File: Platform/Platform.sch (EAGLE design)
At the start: 38 parts, among them U1 FT232RLSSOP, X1 USBSMD, Y1 RESONATORSMD

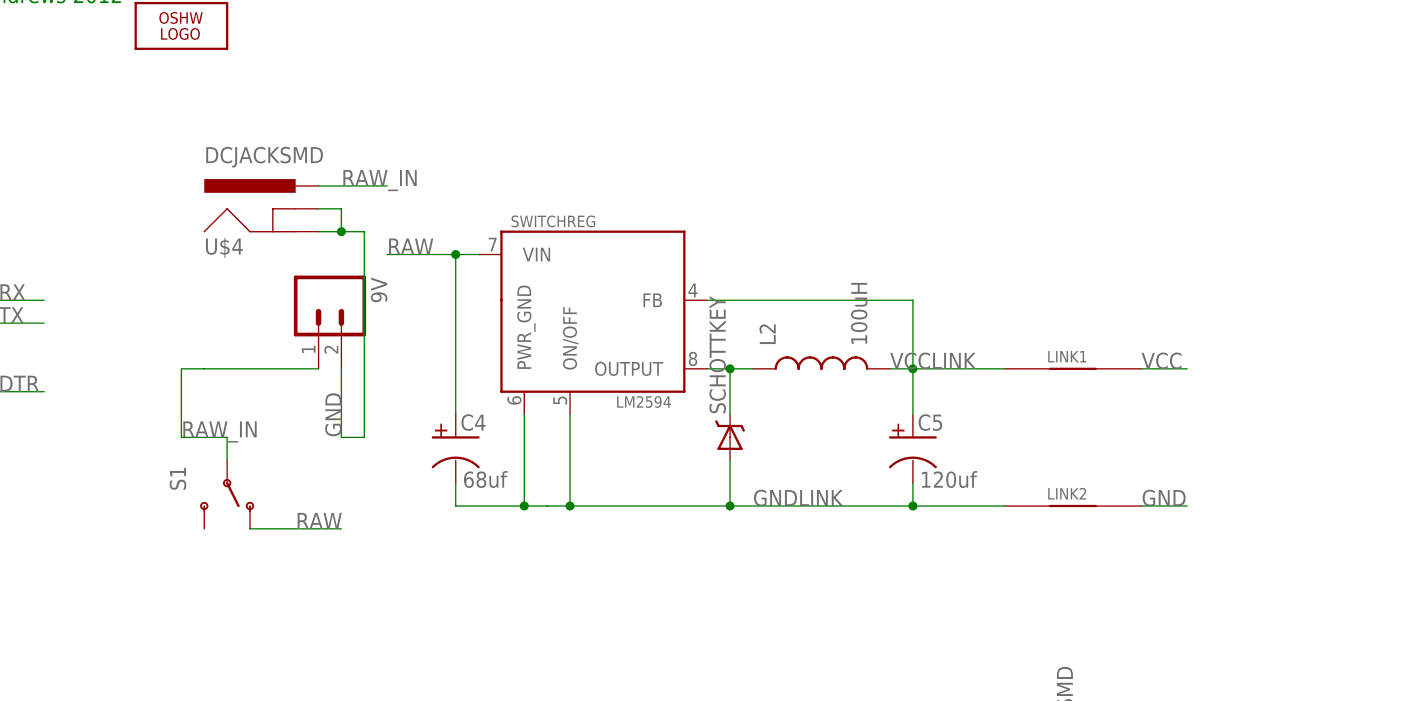
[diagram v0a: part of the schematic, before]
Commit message: switched back to LDO
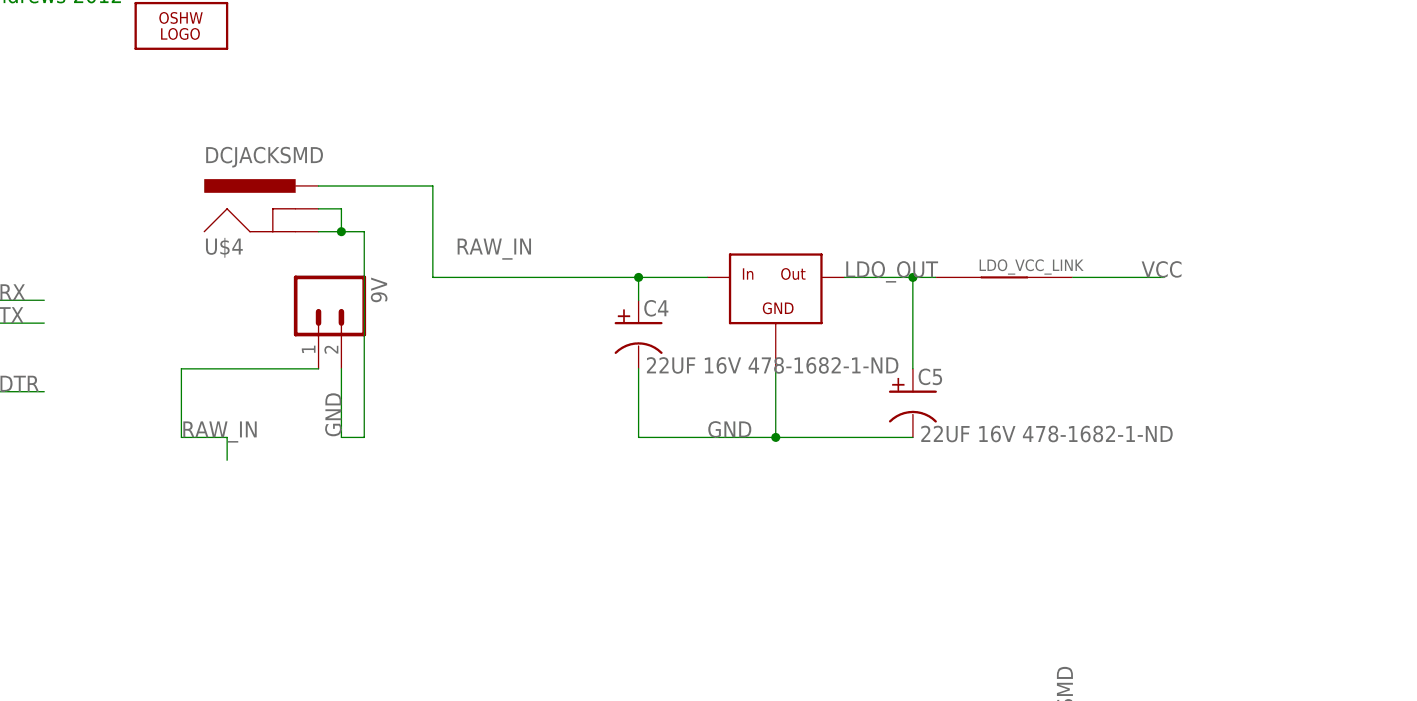
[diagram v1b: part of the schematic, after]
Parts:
- removed L2: 100uH, SparkFun:INDUCTOR0805
- removed LINK1, LINK2: LINK, Dustin:LINK
- removed S1: SWITCH-SPDT, Dustin:SWITCH-SPDT
- removed SCHOTTKEY: DIODE-SCHOTTKY, Dustin:DIODE-SCHOTTKY
- removed SWITCHREG: LM2594, Dustin:LM2594
- added LDO_VCC_LINK: LINK, Dustin:LINK
- added U$1: IFX25001TC, Dustin:IFX25001TC
- C4: value 68uf -> 22UF 16V 478-1682-1-ND; device Dustin:CAP_POLF80 -> Dustin:CAP_POL1210
- C5: value 120uf -> 22UF 16V 478-1682-1-ND; device Dustin:CAP_POL8X10 -> Dustin:CAP_POL1210
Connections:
- removed net GNDLINK: C4.-, C5.-, LINK2.P$1, SCHOTTKEY.A, SWITCHREG.ON/OFF, SWITCHREG.PWR_GND
- removed net N$3: L2.1, SCHOTTKEY.C, SWITCHREG.OUTPUT
- removed net RAW: C4.+, S1.O, SWITCHREG.VIN
- removed net VCCLINK: C5.+, L2.2, LINK1.P$1, SWITCHREG.FB
- new net LDO_OUT: C5.+, LDO_VCC_LINK.P$1, U$1.OUT
- net GND: now also C4.-, C5.-, U$1.GND; no longer LINK2.P$2
- net RAW_IN: now also C4.+, U$1.IN; no longer S1.P
- net VCC: now also LDO_VCC_LINK.P$2; no longer LINK1.P$2
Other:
- moved on the sheet: C4, C5

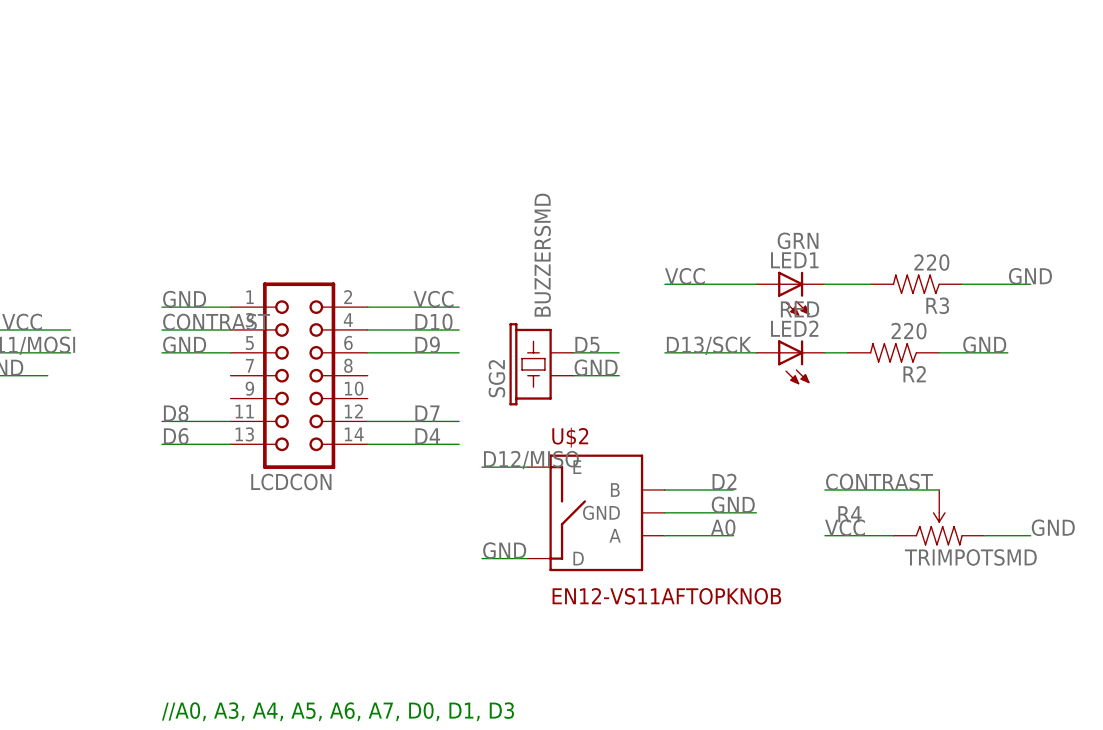
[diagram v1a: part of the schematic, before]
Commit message: wiring traces added
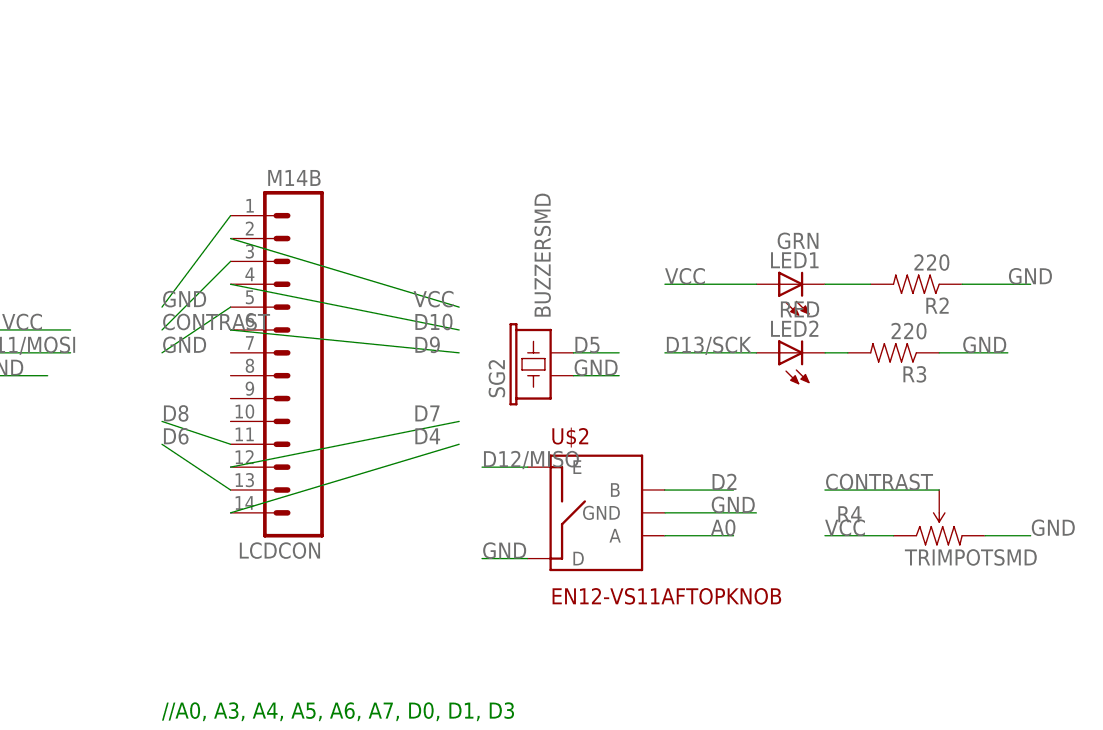
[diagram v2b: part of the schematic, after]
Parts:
- LCDCON: value (none) -> M14B; device con-harting:CON14 -> Dustin:M14B
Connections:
- net N$2: now also R3.2; no longer R2.2
- net N$7: now also R2.2; no longer R3.2
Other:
- moved on the sheet: LCDCON, R2, R3
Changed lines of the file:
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@@
 <part name="L1" library="SparkFun" deviceset="INDUCTOR" device="0805" value="10uH"/>
 <part name="U$2" library="Dustin" deviceset="EN12-VS11AF" device="TOPKNOB"/>
-<part name="R2" library="SparkFun" deviceset="RESISTOR" device="0805-RES" value="220"/>
+<part name="R3" library="SparkFun" deviceset="RESISTOR" device="0805-RES" value="220"/>
 <part name="SPI" library="SparkFun" deviceset="AVR_SPI_PRG_6" device="NS"/>
 <part name="JP2" library="Dustin" deviceset="M14B" device=""/>
@@
 <part name="LED2" library="SparkFun" deviceset="LED" device="0805" value="RED"/>
 <part name="R4" library="SparkFun" deviceset="TRIMPOT" device="SMD"/>
-<part name="LCDCON" library="con-harting" deviceset="CON14" device=""/>
+<part name="LCDCON" library="Dustin" deviceset="M14B" device=""/>
 <part name="LED1" library="SparkFun" deviceset="LED" device="0805" value="GRN"/>
-<part name="R3" library="SparkFun" deviceset="RESISTOR" device="0805-RES" value="220"/>
+<part name="R2" library="SparkFun" deviceset="RESISTOR" device="0805-RES" value="220"/>
 <part name="FTDIVCCLINK" library="Dustin" deviceset="LINK" device=""/>
 <part name="FTDIDGNDLINK" library="Dustin" deviceset="LINK" device=""/>
@@
 <instance part="L1" gate="G$1" x="22.86" y="73.66" rot="R180"/>
 <instance part="U$2" gate="G$1" x="208.28" y="76.2"/>
-<instance part="R2" gate="G$1" x="241.3" y="93.98" rot="R180"/>
+<instance part="R3" gate="G$1" x="241.3" y="93.98" rot="R180"/>
 <instance part="SPI" gate="G$1" x="124.46" y="93.98"/>
 <instance part="JP2" gate="G$1" x="160.02" y="27.94" rot="MR180"/>
@@
 <instance part="LCDCON" gate="G$1" x="175.26" y="91.44" rot="R180"/>
 <instance part="LED1" gate="G$1" x="228.6" y="101.6" rot="R90"/>
-<instance part="R3" gate="G$1" x="243.84" y="101.6" rot="R180"/>
+<instance part="R2" gate="G$1" x="243.84" y="101.6" rot="R180"/>
 <instance part="FTDIVCCLINK" gate="G$1" x="55.88" y="170.18"/>
 <instance part="FTDIDGNDLINK" gate="G$1" x="7.62" y="121.92"/>
@@
 <segment>
 <pinref part="LCDCON" gate="G$1" pin="2"/>
-<wire x1="182.88" y1="99.06" x2="193.04" y2="99.06" width="0.1524" layer="91"/>
+<wire x1="167.64" y1="106.68" x2="193.04" y2="99.06" width="0.1524" layer="91"/>
 <label x="187.96" y="99.06" size="1.778" layer="95"/>
 </segment>
@@
 </segment>
 <segment>
-<pinref part="R2" gate="G$1" pin="1"/>
+<pinref part="R3" gate="G$1" pin="1"/>
 <wire x1="246.38" y1="93.98" x2="254" y2="93.98" width="0.1524" layer="91"/>
 <label x="248.92" y="93.98" size="1.778" layer="95"/>
@@
 <segment>
 <pinref part="LCDCON" gate="G$1" pin="1"/>
-<wire x1="167.64" y1="99.06" x2="160.02" y2="99.06" width="0.1524" layer="91"/>
+<wire x1="167.64" y1="109.22" x2="160.02" y2="99.06" width="0.1524" layer="91"/>
 <label x="160.02" y="99.06" size="1.778" layer="95"/>
 </segment>
 <segment>
 <pinref part="LCDCON" gate="G$1" pin="5"/>
-<wire x1="167.64" y1="93.98" x2="160.02" y2="93.98" width="0.1524" layer="91"/>
+<wire x1="167.64" y1="99.06" x2="160.02" y2="93.98" width="0.1524" layer="91"/>
 <label x="160.02" y="93.98" size="1.778" layer="95"/>
 </segment>
 <segment>
-<pinref part="R3" gate="G$1" pin="1"/>
+<pinref part="R2" gate="G$1" pin="1"/>
 <wire x1="248.92" y1="101.6" x2="256.54" y2="101.6" width="0.1524" layer="91"/>
 <label x="254" y="101.6" size="1.778" layer="95"/>
@@
 <segment>
 <pinref part="LCDCON" gate="G$1" pin="14"/>
-<wire x1="182.88" y1="83.82" x2="193.04" y2="83.82" width="0.1524" layer="91"/>
+<wire x1="167.64" y1="76.2" x2="193.04" y2="83.82" width="0.1524" layer="91"/>
 <label x="187.96" y="83.82" size="1.778" layer="95"/>
 </segment>
@@
 <segment>
 <pinref part="LCDCON" gate="G$1" pin="13"/>
-<wire x1="167.64" y1="83.82" x2="160.02" y2="83.82" width="0.1524" layer="91"/>
+<wire x1="167.64" y1="78.74" x2="160.02" y2="83.82" width="0.1524" layer="91"/>
 <label x="160.02" y="83.82" size="1.778" layer="95"/>
 </segment>
@@
 <segment>
 <pinref part="LCDCON" gate="G$1" pin="12"/>
-<wire x1="182.88" y1="86.36" x2="193.04" y2="86.36" width="0.1524" layer="91"/>
+<wire x1="167.64" y1="81.28" x2="193.04" y2="86.36" width="0.1524" layer="91"/>
 <label x="187.96" y="86.36" size="1.778" layer="95"/>
 </segment>
@@
 <segment>
 <pinref part="LCDCON" gate="G$1" pin="11"/>
-<wire x1="167.64" y1="86.36" x2="160.02" y2="86.36" width="0.1524" layer="91"/>
+<wire x1="167.64" y1="83.82" x2="160.02" y2="86.36" width="0.1524" layer="91"/>
 <label x="160.02" y="86.36" size="1.778" layer="95"/>
 </segment>
@@
 <segment>
 <pinref part="LCDCON" gate="G$1" pin="6"/>
-<wire x1="182.88" y1="93.98" x2="193.04" y2="93.98" width="0.1524" layer="91"/>
+<wire x1="167.64" y1="96.52" x2="193.04" y2="93.98" width="0.1524" layer="91"/>
 <label x="187.96" y="93.98" size="1.778" layer="95"/>
 </segment>
@@
 <segment>
 <pinref part="LCDCON" gate="G$1" pin="4"/>
-<wire x1="182.88" y1="96.52" x2="193.04" y2="96.52" width="0.1524" layer="91"/>
+<wire x1="167.64" y1="101.6" x2="193.04" y2="96.52" width="0.1524" layer="91"/>
 <label x="187.96" y="96.52" size="1.778" layer="95"/>
 </segment>
@@
 <net name="N$2" class="0">
 <segment>
-<pinref part="R2" gate="G$1" pin="2"/>
+<pinref part="R3" gate="G$1" pin="2"/>
 <wire x1="236.22" y1="93.98" x2="233.68" y2="93.98" width="0.1524" layer="91"/>
 <pinref part="LED2" gate="G$1" pin="C"/>
@@
 <segment>
 <pinref part="LCDCON" gate="G$1" pin="3"/>
-<wire x1="167.64" y1="96.52" x2="160.02" y2="96.52" width="0.1524" layer="91"/>
+<wire x1="167.64" y1="104.14" x2="160.02" y2="96.52" width="0.1524" layer="91"/>
 <label x="160.02" y="96.52" size="1.778" layer="95"/>
 </segment>
@@
 <segment>
 <pinref part="LED1" gate="G$1" pin="C"/>
-<pinref part="R3" gate="G$1" pin="2"/>
+<pinref part="R2" gate="G$1" pin="2"/>
 <wire x1="238.76" y1="101.6" x2="233.68" y2="101.6" width="0.1524" layer="91"/>
 </segment>

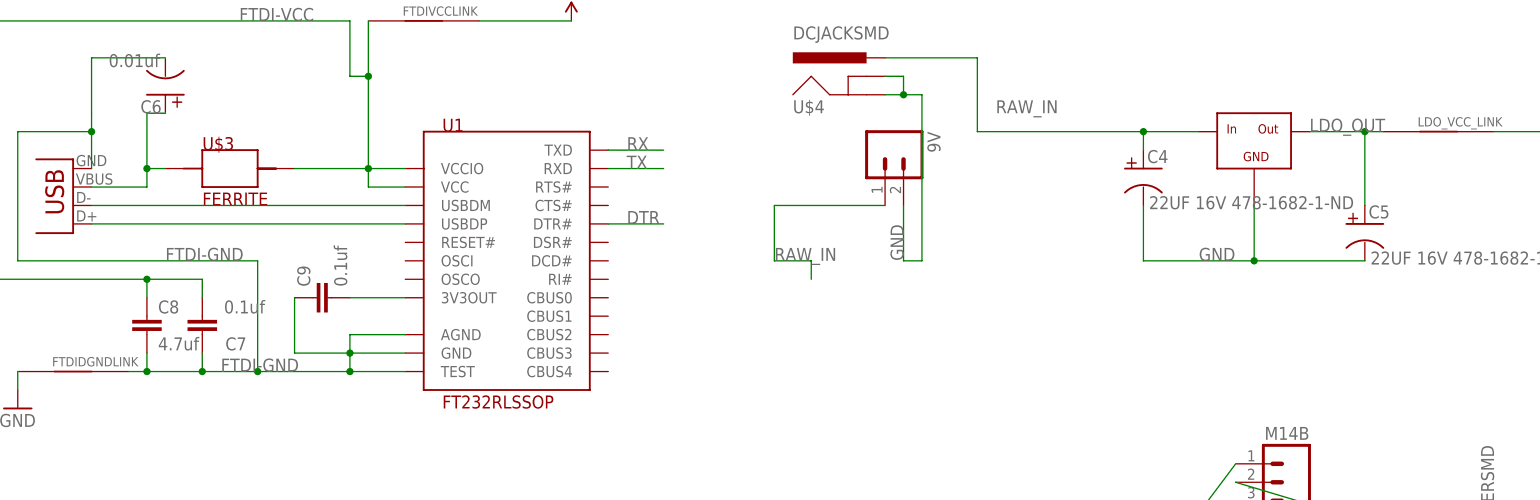
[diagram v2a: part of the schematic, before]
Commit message: Added DIGIKEY# attribute to parts and generated BOM
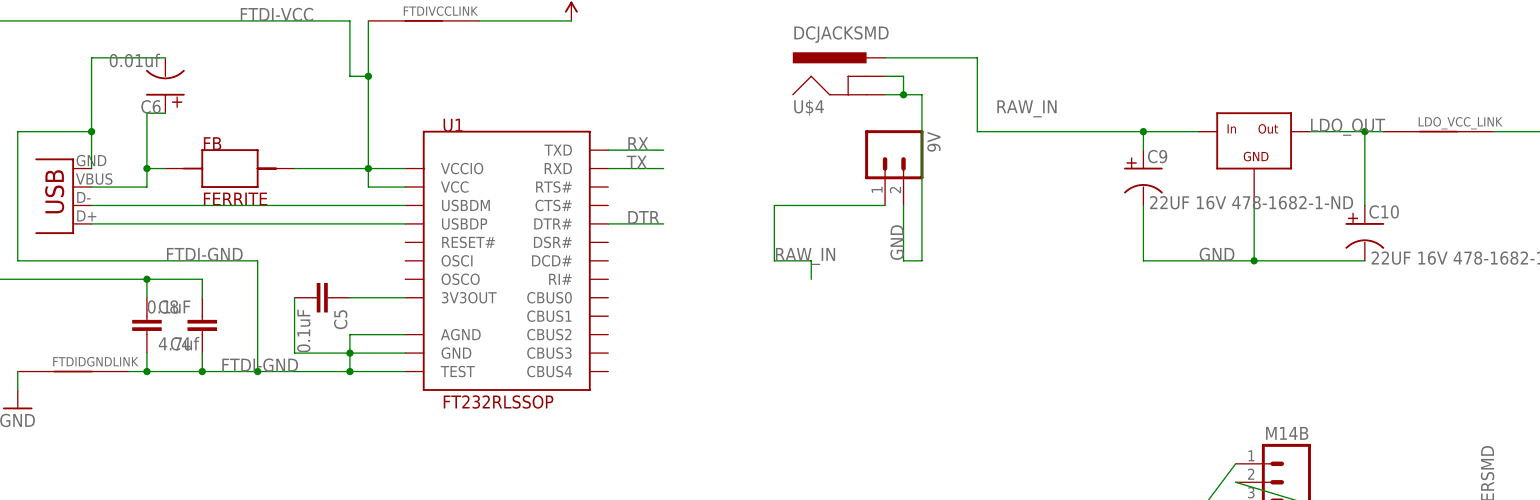
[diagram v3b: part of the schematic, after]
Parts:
- removed C7: 0.1uf, SparkFun:CAP0805
- added C10: 22UF 16V 478-1682-1-ND, Dustin:CAP_POL1210
- ATMEGAXX8: DIGIKEY# (none) -> ATMEGA328-AU
- C1, C2, C3: DIGIKEY# (none) -> 478-1395-1-ND
- C4, C5: value 22UF 16V 478-1682-1-ND -> 0.1uF; device Dustin:CAP_POL1210 -> SparkFun:CAP0805; DIGIKEY# (none) -> 478-1395-1-ND
- C6: DIGIKEY# (none) -> 478-1383-1-ND
- C8: DIGIKEY# (none) -> 445-1369-1-ND
- C9: value 0.1uf -> 22UF 16V 478-1682-1-ND; device SparkFun:CAP0805 -> Dustin:CAP_POL1210; DIGIKEY# (none) -> 478-1682-1-ND
- FB: DIGIKEY# (none) -> 240-2399-1-ND
- L1: DIGIKEY# (none) -> 587-2048-1-ND
- LCDCON, LED1: DIGIKEY# (none) -> 754-1131-1-ND
- LED2: DIGIKEY# (none) -> 475-1278-1-ND
- R1: DIGIKEY# (none) -> RHM10.0KAECT-ND
- R2, R3: DIGIKEY# (none) -> RHM220AECT-ND
- R4: DIGIKEY# (none) -> 490-4611-1-ND
- SG2: DIGIKEY# (none) -> 668-1110-1-ND
- U$1: DIGIKEY# (none) -> IFX25001TC V50INCT-ND
- U$2: DIGIKEY# (none) -> 987-1194-ND
- U$4: DIGIKEY# (none) -> CP-002APJCT-ND
- U1: DIGIKEY# (none) -> 768-1007-1-ND
- X1: DIGIKEY# (none) -> ED2992CT-ND
- Y1: DIGIKEY# (none) -> 490-1198-1-ND
- renumbered U$3 to FB
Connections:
- net 3V3OUT: now also C5.1; no longer C9.2
- net FTDI-GND: now also C4.1, C5.2; no longer C7.1, C9.1
- net FTDI-VCC: now also C4.2; no longer C7.2
- net GND: now also C10.-, C9.-; no longer C4.-, C5.-
- net LDO_OUT: now also C10.+; no longer C5.+
- net RAW_IN: now also C9.+; no longer C4.+

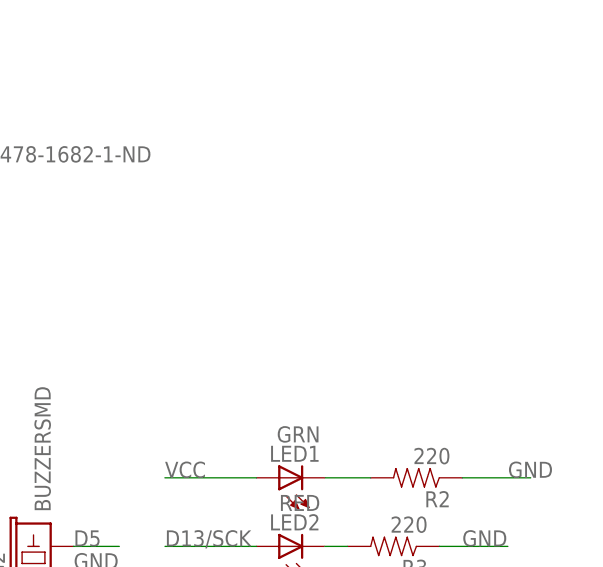
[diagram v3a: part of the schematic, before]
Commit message: added dimensions, reference drawing for lcd
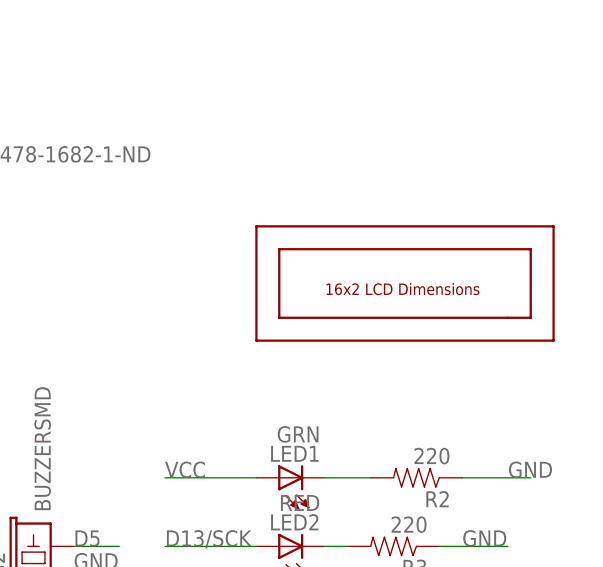
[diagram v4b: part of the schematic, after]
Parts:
- added U$3: LCM-S01602DTR, Dustin:LCM-S01602DTR
- LCDCON: DIGIKEY# 754-1131-1-ND -> 67-1781-ND
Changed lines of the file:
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@@
 </part>
 <part name="LCDCON" library="Dustin" deviceset="M14B" device="">
-<attribute name="DIGIKEY#" value="754-1131-1-ND"/>
+<attribute name="DIGIKEY#" value="67-1781-ND"/>
 </part>
 <part name="LED1" library="SparkFun" deviceset="LED" device="0805" value="GRN">
@@
 <attribute name="DIGIKEY#" value="478-1395-1-ND"/>
 </part>
+<part name="U$3" library="Dustin" deviceset="LCM-S01602DTR" device=""/>
 </parts>
 <sheets>
@@
 <attribute name="DIGIKEY#" x="40.64" y="132.08" size="1.778" layer="96" rot="R270" display="off"/>
 </instance>
+<instance part="U$3" gate="G$1" x="226.06" y="116.84"/>
 </instances>
 <busses>
